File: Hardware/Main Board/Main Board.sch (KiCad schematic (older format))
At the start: 51 parts, among them Q1 NPN, Q2 NPN, Q3 A04484, SW1 Momentary, U1 MC33063AD, U2 NCP718A, U3 ATtiny20-CCU

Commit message: Updated DC-DC design, updated MCU and added datasheets
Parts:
- removed C?: 100pf, symbol Device:CP1_Small
- removed C?: 470uf, symbol Device:CP1_Small
- removed C?: 100uf, symbol Device:CP1_Small
- removed D?: 1N5819, symbol Device:D_Zener
- removed L?: 23uh, symbol Device:L_Core_Iron
- removed R?: 3k, symbol Device:R_Small
- removed R?: 24k, symbol Device:R_Small
- removed R?: 180, symbol Device:R_Small
- removed R?: 20mohm, symbol Device:R_Small
- removed U3: ATtiny20-CCU, Package_BGA:UFBGA-15_3.0x3.0mm_Layout4x4_P0.65mm, symbol Main-Board-rescue:ATtiny20-CCU-MCU_Microchip_ATtiny
- removed U?: MC33063AD, Package_SO:SOIC-8_3.9x4.9mm_P1.27mm, symbol Regulator_Switching:MC33063AD
- added C12, C4: uf, symbol Device:C_Small
- added D2: 1N5819, symbol Device:D_Zener
- added L2: 23uh, symbol Device:L_Core_Iron
- added R15, R16: 3k, symbol Device:R_Small
- added U4: MT3608, symbol New_Library:MT3608
- added U?: ATtiny814-SS, Package_SO:SOIC-14_3.9x8.7mm_P1.27mm, symbol MCU_Microchip_ATtiny:ATtiny814-SS
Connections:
- net labels added: PACK_SENSE, POWER, PRMG, TEMP_SENSE
- wire segments 115 -> 113
- no-connect marks 0 -> 1
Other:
- moved on the sheet: C10, C11

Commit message: datasheeets
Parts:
- added D?: 1N5819, symbol Device:D_Zener
- added D?: ???, symbol Device:D_Zener
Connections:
- net +5V: now also D?.1 (K), D?.1 (K); no longer C9.1, R12.1, U2.5 (VOUT)
- net +BATT: now also D?.2 (A)
- new net: C9.1, D?.2 (A), R12.1, U2.5 (VOUT)
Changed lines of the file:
@@
 	1    0    0    -1
 $EndComp
-Connection ~ 4620 2250
 $Comp
 L power:+5V #PWR016
@@
 $EndComp
 Wire Wire Line
-	5140 1790 5140 2250
-Wire Wire Line
 	950  2790 950  2990
 Wire Wire Line
@@
 Text Label 1940 5760 2    50   ~ 0
 MODE
-Wire Wire Line
-	3020 1800 3020 2250
 Connection ~ 3020 2250
 Wire Wire Line
@@
 	8400 3345 8400 2935
 Wire Wire Line
-	4620 2250 5140 2250
-Wire Wire Line
 	8400 2935 7495 2935
 Wire Wire Line
@@
 Text Label 9465 3645 2    50   ~ 0
 PRMG
+$Comp
+L Device:D_Zener D?
+U 1 1 5EDA6065
+P 4060 1430
+F 0 "D?" H 4100 1160 50  0000 R CNN
+F 1 "1N5819" H 4175 1295 50  0000 R CNN
+F 2 "" H 4060 1430 50  0001 C CNN
+F 3 "~" H 4060 1430 50  0001 C CNN
+	1    4060 1430
+	-1   0    0    1
+$EndComp
+Wire Wire Line
+	3020 1800 3020 2250
+Wire Wire Line
+	5140 1790 5140 2250
+Wire Wire Line
+	4210 1430 4210 1790
+Wire Wire Line
+	4210 1790 5140 1790
+Connection ~ 5140 1790
+Wire Wire Line
+	3910 1430 1165 1430
+Wire Wire Line
+	1165 1430 1165 1780
+Wire Wire Line
+	1165 1780 940  1780
+Connection ~ 940  1780
+$Comp
+L Device:D_Zener D?
+U 1 1 5EDD461B
+P 4905 2250
+F 0 "D?" H 4945 2055 50  0000 R CNN
+F 1 "???" H 4965 2155 50  0000 R CNN
+F 2 "" H 4905 2250 50  0001 C CNN
+F 3 "~" H 4905 2250 50  0001 C CNN
+	1    4905 2250
+	-1   0    0    1
+$EndComp
+Wire Wire Line
+	4620 2250 4755 2250
+Connection ~ 4620 2250
+Wire Wire Line
+	5055 2250 5140 2250
+Text Label 4835 2390 0    50   ~ 0
+test_this
+Text Label 5315 4350 0    50   ~ 0
+1
+Text Label 5320 4490 0    50   ~ 0
+2
+Text Label 5290 4765 0    50   ~ 0
+3
+Text Label 6005 4705 0    50   ~ 0
+6
+Text Label 6050 4505 0    50   ~ 0
+7
+Text Label 5990 4305 0    50   ~ 0
+8
+Text Label 6465 3720 0    50   ~ 0
+input
+Text Label 4740 3660 0    50   ~ 0
+output
 $EndSCHEMATC

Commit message: Huge changes to schematic!
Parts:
- removed C6: 100pf, symbol Device:CP1_Small
- removed C7: 470uf, symbol Device:CP1_Small
- removed D?: 1N5819, symbol Device:D_Zener
- removed L1: 23uh, symbol Device:L_Core_Iron
- removed R10: 180, symbol Device:R_Small
- removed R11: 24k, symbol Device:R_Small
- removed R9: 20mohm, symbol Device:R_Small
- removed U1: MC33063AD, Package_SO:SOIC-8_3.9x4.9mm_P1.27mm, symbol Regulator_Switching:MC33063AD
- added FB1: ?, symbol Device:Ferrite_Bead_Small
- added L2: 1uh, symbol Device:L_Core_Iron
- C12, C4: value uf -> 22uf
- D3: renamed from D?; value ??? -> 1N5819
- L1: renamed from L2; value 23uh -> 10uh
- R15: value 3k -> 43k
- R16: value 3k -> 2.7k
- R8: value 3k -> 1M
- gave numbers to parts that had none: 1
- renumbered U4 to U1
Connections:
- net labels added: +10V, GNDA, GNDPWR, MAIN_POWER, Supply_Detect
- net labels removed: +12V, 1, 2, 3, 6, 7, 8, GND, POWER, Test_This!, input, output, test_this
- wire segments 119 -> 115
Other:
- note added: "Design Requirements:\n\nR15 & R16 Close to U1. Feedback line short as possible. Short and wide traces\n\nC8 & C9 close to U2\n\nC10 & C11 close to U3\n\n"
- note added: "Flake Technologies (?)\n"
- note added: "Michael Madi\n"
- note added: "Rave Lights Main Board\n"
- note removed: "Design Requirements:\n\nC9 close to U2\nC10 & C11 close to U3\nFeedback line on U1 as short as possible"
- note removed: "Power Delivery\n"
- moved on the sheet: C1, C10, C11, C12, C2, C3, C4, C8, C9, D2, D3, L1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

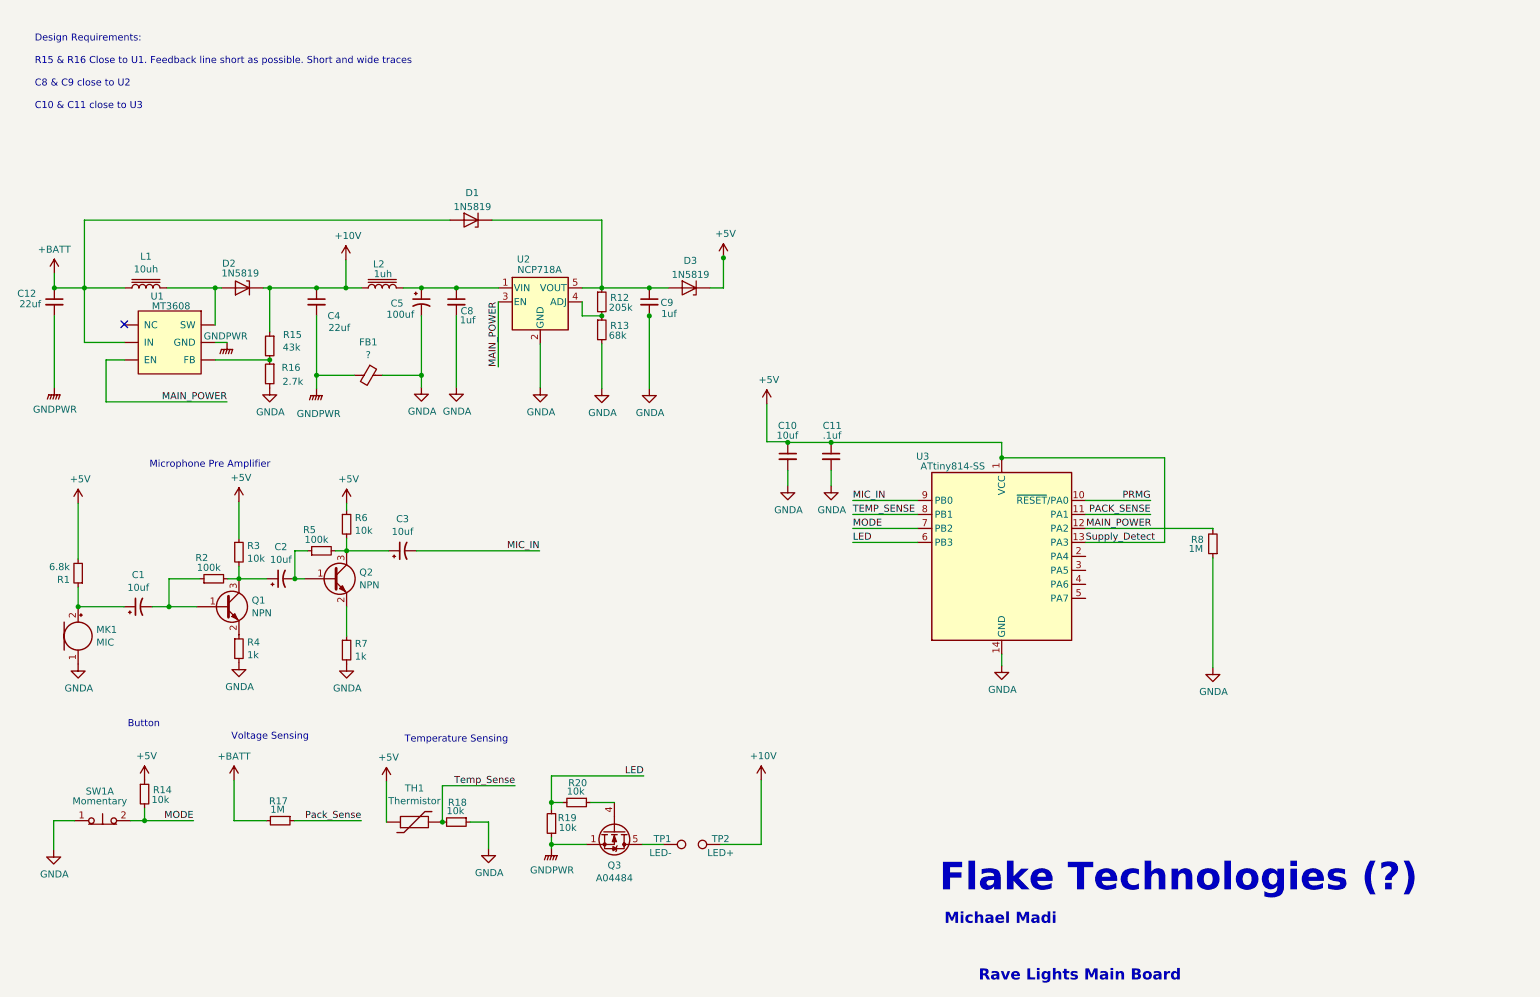
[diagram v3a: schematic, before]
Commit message: Added JTAG programming interface and decoupling cap on amp supply
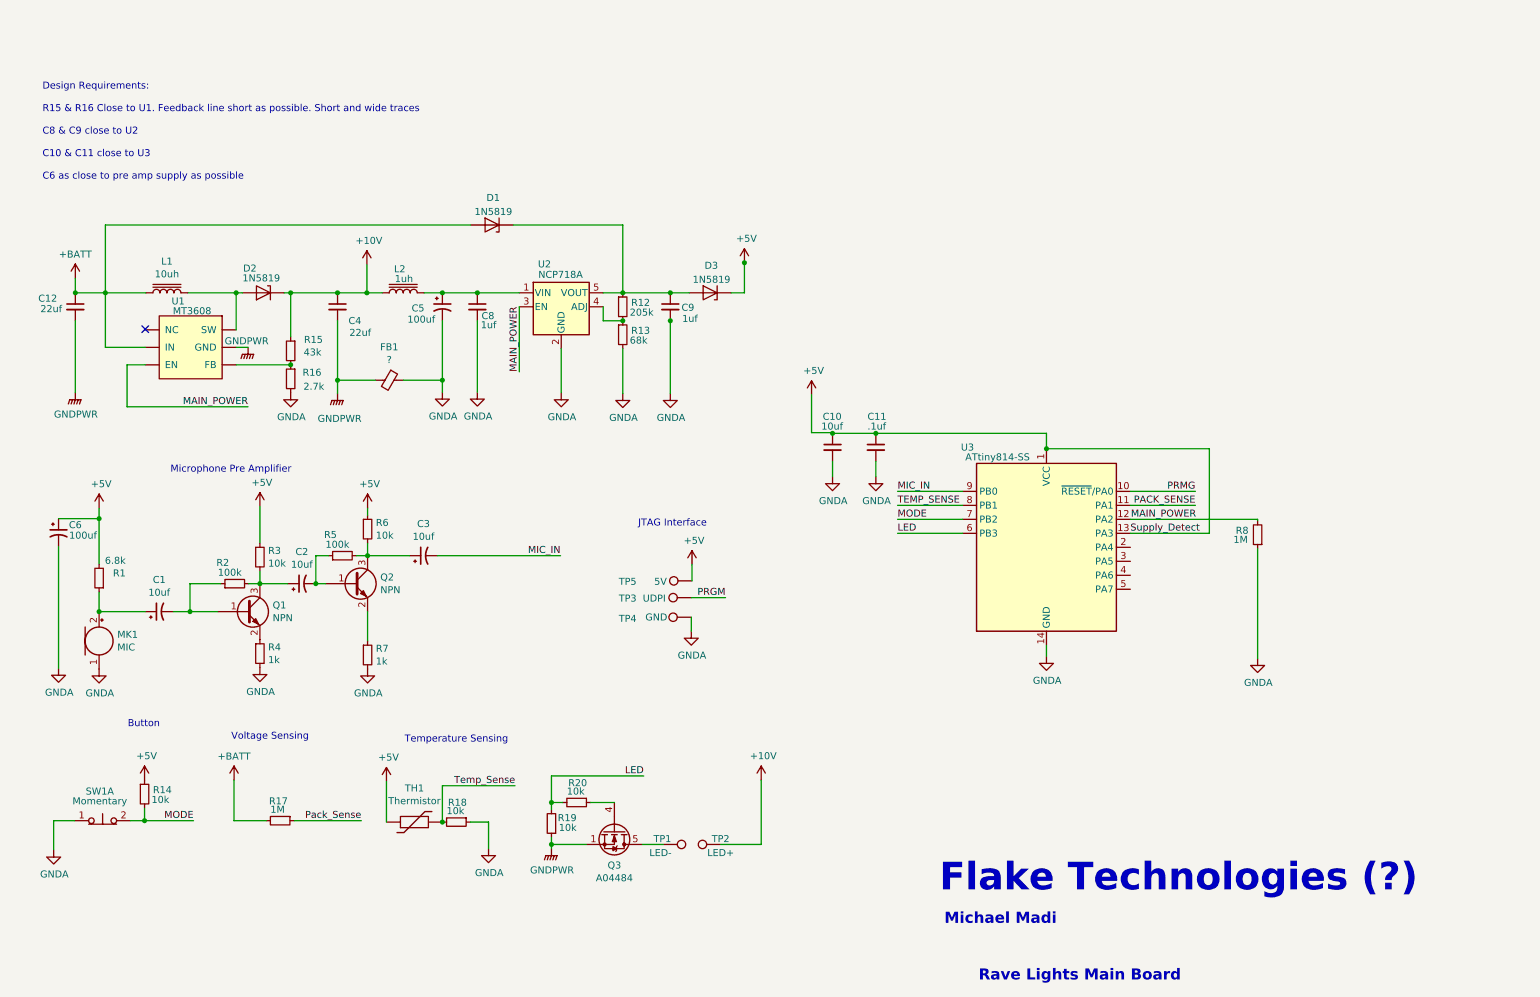
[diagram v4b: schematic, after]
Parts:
- added C6: 100uf, symbol Device:CP1_Small
- added TP3: UDPI, symbol Connector:TestPoint
- added TP4: GND, symbol Connector:TestPoint
- added TP5: 5V, symbol Connector:TestPoint
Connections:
- net labels added: PRGM
- wire segments 115 -> 121
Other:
- note added: "Design Requirements:\n\nR15 & R16 Close to U1. Feedback line short as possible. Short and wide traces\n\nC8 & C9 close to U2\n\nC10 & C11 close to U3\n\nC6 as close to pre amp supply as possible\n\n"
- note added: "JTAG Interface \n"
- note removed: "Design Requirements:\n\nR15 & R16 Close to U1. Feedback line short as possible. Short and wide traces\n\nC8 & C9 close to U2\n\nC10 & C11 close to U3\n\n"
- moved on the sheet: C1, C10, C11, C12, C2, C3, C4, C5, C8, C9, D1, D2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

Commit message: .
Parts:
- added R9: 1M, symbol Device:R_Small
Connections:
- net labels added: SUPPLY_DETECT
- net labels removed: Supply_Detect
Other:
- note added: "Dynamic Power Delivery"
- moved on the sheet: C10, C11, R8, TP3, TP4, TP5, U3

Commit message: .
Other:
- note added: "Michael Madi | David Roberts\n\n"
- note removed: "Michael Madi\n"
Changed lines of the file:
@@
 Text Notes 7070 6880 0    197  ~ 39
 Flake Technologies (?)\n
-Text Notes 7105 7105 0    79   ~ 16
-Michael Madi\n
+Text Notes 7100 7250 0    79   ~ 16
+Michael Madi | David Roberts\n\n
 Text Notes 7350 7510 0    79   ~ 16
 Rave Lights Main Board\n

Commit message: started core functions code
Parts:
- R20: value 10k -> 220R
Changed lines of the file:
@@
 P 4475 6225
 F 0 "R20" V 4335 6165 50  0000 L CNN
-F 1 "10k" V 4395 6155 50  0000 L CNN
+F 1 "220R" V 4395 6155 50  0000 L CNN
 F 2 "" H 4475 6225 50  0001 C CNN
 F 3 "~" H 4475 6225 50  0001 C CNN

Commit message: minor adjustments
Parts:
- removed R9: 1M, symbol Device:R_Small
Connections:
- net SUPPLY_DETECT: no longer names the net of U3.13 (PA3)
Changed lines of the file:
@@
 	1    0    0    -1
 $EndComp
-Wire Wire Line
-	8625 4300 8625 3695
-Text Label 8010 4300 0    50   ~ 0
-SUPPLY_DETECT
-$Comp
-L MCU_Microchip_ATtiny:ATtiny814-SS U3
-U 1 1 5EE6BDE9
-P 7410 4400
-F 0 "U3" H 6845 5115 50  0000 C CNN
-F 1 "ATtiny814-SS" H 7060 5045 50  0000 C CNN
-F 2 "Package_SO:SOIC-14_3.9x8.7mm_P1.27mm" H 7410 4400 50  0001 C CIN
-F 3 "http://ww1.microchip.com/downloads/en/DeviceDoc/40001912A.pdf" H 7410 4400 50  0001 C CNN
-	1    7410 4400
-	1    0    0    -1
-$EndComp
-Wire Wire Line
-	7410 3695 7410 3700
-Wire Wire Line
-	7410 3585 7410 3695
-Connection ~ 7410 3695
 $Comp
 L Device:CP1_Small C6
@@
 Text Notes 2225 1980 0    50   ~ 0
 Dynamic Power Delivery
-$Comp
-L Device:R_Small R9
-U 1 1 5EEC31AD
-P 7940 3695
-F 0 "R9" V 7800 3615 50  0000 L CNN
-F 1 "1M" V 7860 3625 50  0000 L CNN
-F 2 "" H 7940 3695 50  0001 C CNN
-F 3 "~" H 7940 3695 50  0001 C CNN
-	1    7940 3695
-	0    1    1    0
-$EndComp
-Wire Wire Line
-	7840 3695 7410 3695
 Wire Wire Line
 	5675 2360 5675 2580
@@
 Wire Wire Line
 	890  2350 890  2580
-Wire Wire Line
-	8040 3695 8625 3695
-Wire Wire Line
-	8010 4300 8625 4300
 Text Notes 590  1380 0    50   ~ 0
 Design Requirements:\n\nR15 & R16 Close to U1. Feedback line short as possible. Short and wide traces\n\nC8 & C9 close to U2\n\nC10 & C11 close to U3\n\nC6 as close to pre amp supply as possible\n\n
+$Comp
+L MCU_Microchip_ATtiny:ATtiny814-SS U3
+U 1 1 5EE6BDE9
+P 7410 4400
+F 0 "U3" H 6845 5115 50  0000 C CNN
+F 1 "ATtiny814-SS" H 7060 5045 50  0000 C CNN
+F 2 "Package_SO:SOIC-14_3.9x8.7mm_P1.27mm" H 7410 4400 50  0001 C CIN
+F 3 "http://ww1.microchip.com/downloads/en/DeviceDoc/40001912A.pdf" H 7410 4400 50  0001 C CNN
+	1    7410 4400
+	1    0    0    -1
+$EndComp
+Wire Wire Line
+	7410 3585 7410 3700
 $EndSCHEMATC
